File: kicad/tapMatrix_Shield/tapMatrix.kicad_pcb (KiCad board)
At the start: 2 copper layers, 68.6 x 53.3 mm, 28 parts, among them IC1 DS1307, P5 TS_ZIF, P6 LED_MATRIX_HDR, P7 SPKR, U1 APE8865N-33-HF-3, U2 MCP4921-E/SN, U3 74LS125, U4 TL072, U5 SD_CARD

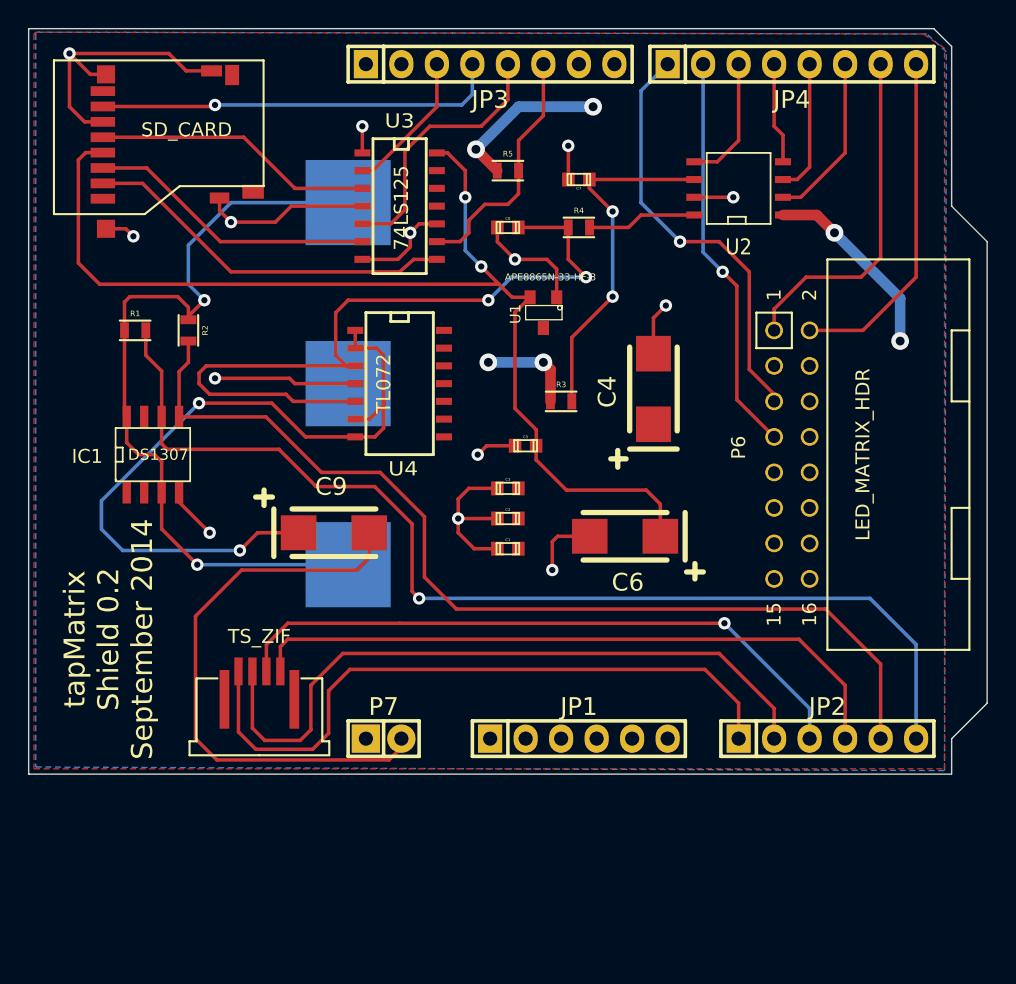
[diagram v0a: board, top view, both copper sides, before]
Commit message: added optional 4-pin header as alt for touchscreen zif
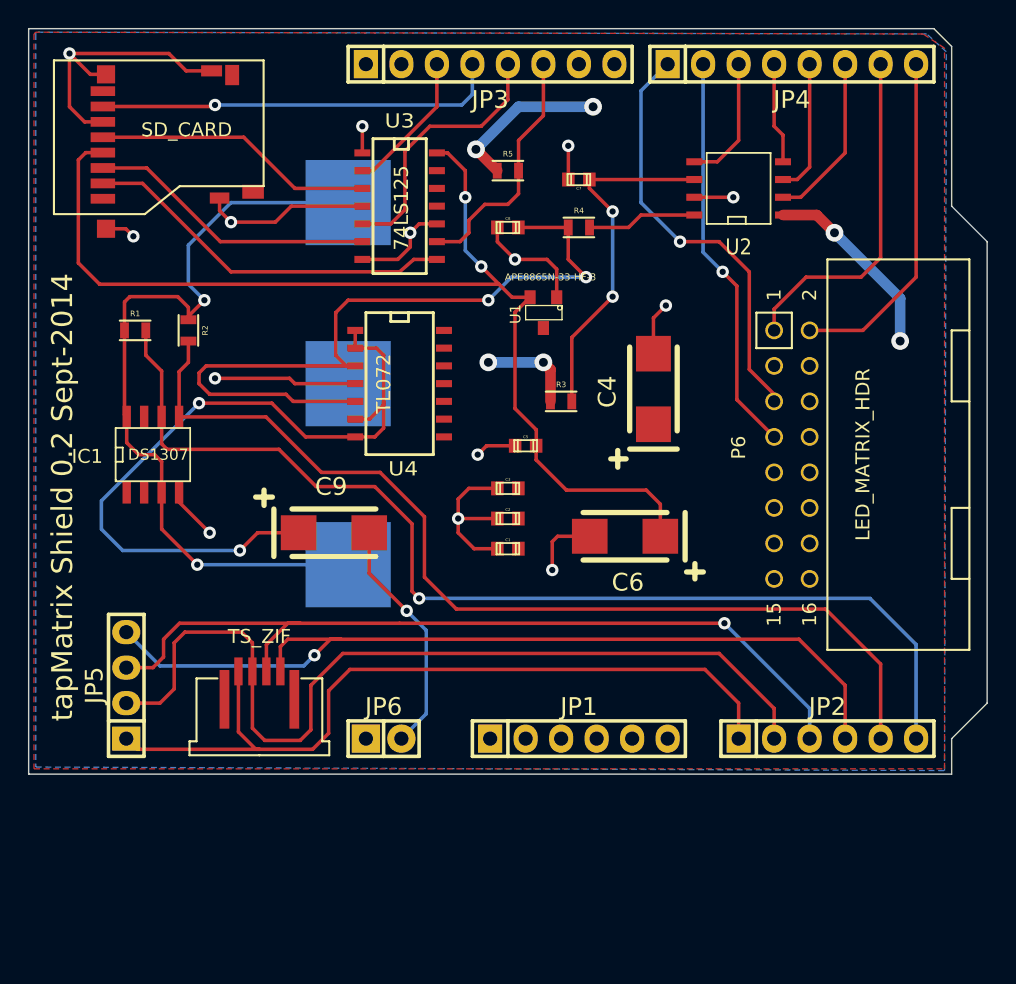
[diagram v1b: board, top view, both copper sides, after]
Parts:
- added JP5: 4_PIN_1, Pin_Headers:Pin_Header_Straight_1x04, F.Cu at (137.8, 133.3)
- renumbered P7 to JP6
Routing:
- net Net-(C9-Pad2): track 41.1 -> 17.8 mm, vias 0 -> 1
- net /YM: track 47.6 -> 64.7 mm, vias 0 -> 1
- net /YP: track 50.0 -> 65.4 mm
- net /XP: track 47.1 -> 61.6 mm
- net /XM: track 48.3 -> 58.2 mm
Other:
- board text added: "tapMatrix Shield 0.2 Sept-2014"
- board text removed: "tapMatrix Shield 0.2 September 2014"
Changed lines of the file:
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@@
 (kicad_pcb (version 4) (host pcbnew "(2014-08-05 BZR 5054)-product")
   (general
-    (links 85)
+    (links 89)
     (no_connects 0)
     (area 130.759999 86.309999 199.440001 139.750001)
     (thickness 1.6)
     (drawings 98)
-    (tracks 319)
+    (tracks 340)
     (zones 0)
-    (modules 28)
+    (modules 29)
     (nets 50)
   )
@@
     (descr "1 pin")
     (tags "CONN DEV")
-    (fp_text reference P7 (at 0 -2.286) (layer F.SilkS)
+    (fp_text reference JP6 (at 0 -2.286) (layer F.SilkS)
       (effects (font (size 1.27 1.27) (thickness 0.2032)))
     )
@@
       (net 5 "Net-(C9-Pad1)"))
   )
+  (module Pin_Headers:Pin_Header_Straight_1x04 (layer F.Cu)
+    (at 137.795 133.35 90)
+    (descr "1 pin")
+    (tags "CONN DEV")
+    (fp_text reference JP5 (at 0 -2.286 90) (layer F.SilkS)
+      (effects (font (size 1.27 1.27) (thickness 0.2032)))
+    )
+    (fp_text value 4_PIN_1 (at 0 0 90) (layer F.SilkS) hide
+      (effects (font (size 1.27 1.27) (thickness 0.2032)))
+    )
+    (fp_line (start -2.54 1.27) (end 5.08 1.27) (layer F.SilkS) (width 0.254))
+    (fp_line (start -2.54 -1.27) (end 5.08 -1.27) (layer F.SilkS) (width 0.254))
+    (fp_line (start -5.08 -1.27) (end -2.54 -1.27) (layer F.SilkS) (width 0.254))
+    (fp_line (start 5.08 1.27) (end 5.08 -1.27) (layer F.SilkS) (width 0.254))
+    (fp_line (start -2.54 -1.27) (end -2.54 1.27) (layer F.SilkS) (width 0.254))
+    (fp_line (start -5.08 -1.27) (end -5.08 1.27) (layer F.SilkS) (width 0.254))
+    (fp_line (start -5.08 1.27) (end -2.54 1.27) (layer F.SilkS) (width 0.254))
+    (pad 1 thru_hole rect (at -3.81 0 90) (size 1.7272 2.032) (drill 1.016) (layers *.Cu *.Mask F.SilkS)
+      (net 16 /XM))
+    (pad 2 thru_hole oval (at -1.27 0 90) (size 1.7272 2.032) (drill 1.016) (layers *.Cu *.Mask F.SilkS)
+      (net 17 /YP))
+    (pad 3 thru_hole oval (at 1.27 0 90) (size 1.7272 2.032) (drill 1.016) (layers *.Cu *.Mask F.SilkS)
+      (net 18 /XP))
+    (pad 4 thru_hole oval (at 3.81 0 90) (size 1.7272 2.032) (drill 1.016) (layers *.Cu *.Mask F.SilkS)
+      (net 19 /YM))
+    (model Pin_Headers/Pin_Header_Straight_1x04.wrl
+      (at (xyz 0 0 0))
+      (scale (xyz 1 1 1))
+      (rotate (xyz 0 0 0))
+    )
+  )
   (gr_text "(c) 2014 Responsive Devices Inc" (at 133.35 119.126 90) (layer B.SilkS)
     (effects (font (size 1.5 1.5) (thickness 0.3)) (justify mirror))
   )
-  (gr_text "tapMatrix\nShield 0.2\nSeptember 2014" (at 136.525 130.048 90) (layer F.SilkS)
+  (gr_text "tapMatrix Shield 0.2 Sept-2014" (at 133.223 119.888 90) (layer F.SilkS)
     (effects (font (size 1.5 1.5) (thickness 0.3)))
   )
@@
   (segment (start 156.21 114.935) (end 155.575 115.57) (width 0.254) (layer F.Cu) (net 5))
   (segment (start 155.575 115.57) (end 154.178 115.57) (width 0.254) (layer F.Cu) (net 5))
+  (segment (start 155.17876 122.428) (end 155.17876 125.33376) (width 0.254) (layer F.Cu) (net 6))
+  (segment (start 159.258 135.382) (end 157.48 137.16) (width 0.254) (layer B.Cu) (net 6))
+  (segment (start 159.258 129.413) (end 159.258 135.382) (width 0.254) (layer B.Cu) (net 6))
+  (segment (start 157.861 128.016) (end 159.258 129.413) (width 0.254) (layer B.Cu) (net 6))
+  (via (at 157.861 128.016) (size 0.889) (layers F.Cu B.Cu) (net 6))
+  (segment (start 155.17876 125.33376) (end 157.861 128.016) (width 0.254) (layer F.Cu) (net 6))
   (segment (start 157.48 137.16) (end 157.48 137.795) (width 0.254) (layer F.Cu) (net 6))
-  (segment (start 157.48 137.795) (end 156.591 138.684) (width 0.254) (layer F.Cu) (net 6))
-  (segment (start 156.591 138.684) (end 144.272 138.684) (width 0.254) (layer F.Cu) (net 6))
-  (segment (start 144.272 138.684) (end 142.748 137.16) (width 0.254) (layer F.Cu) (net 6))
-  (segment (start 142.748 137.16) (end 142.748 128.397) (width 0.254) (layer F.Cu) (net 6))
-  (segment (start 142.748 128.397) (end 146.05 125.095) (width 0.254) (layer F.Cu) (net 6))
-  (segment (start 146.05 125.095) (end 154.305 125.095) (width 0.254) (layer F.Cu) (net 6))
-  (segment (start 154.305 125.095) (end 155.17876 124.22124) (width 0.254) (layer F.Cu) (net 6))
-  (segment (start 155.17876 124.22124) (end 155.17876 122.428) (width 0.254) (layer F.Cu) (net 6))
   (segment (start 153.67 98.806) (end 145.288 98.806) (width 0.254) (layer B.Cu) (net 7))
   (segment (start 143.383 105.791) (end 142.24 106.934) (width 0.254) (layer F.Cu) (net 7))
@@
   (segment (start 141.575 110.901) (end 141.575 114.14) (width 0.254) (layer F.Cu) (net 11))
   (segment (start 142.24 110.236) (end 141.575 110.901) (width 0.254) (layer F.Cu) (net 11))
+  (segment (start 147.32 137.922) (end 138.557 137.922) (width 0.254) (layer F.Cu) (net 16))
+  (segment (start 138.557 137.922) (end 137.795 137.16) (width 0.254) (layer F.Cu) (net 16))
   (segment (start 181.61 137.16) (end 181.61 134.62) (width 0.254) (layer F.Cu) (net 16))
   (segment (start 145.82 136.676) (end 145.82 132.35) (width 0.254) (layer F.Cu) (net 16))
   (segment (start 147.066 137.922) (end 145.82 136.676) (width 0.254) (layer F.Cu) (net 16))
-  (segment (start 151.13 137.922) (end 147.066 137.922) (width 0.254) (layer F.Cu) (net 16))
+  (segment (start 151.13 137.922) (end 147.32 137.922) (width 0.254) (layer F.Cu) (net 16))
+  (segment (start 147.32 137.922) (end 147.066 137.922) (width 0.254) (layer F.Cu) (net 16))
   (segment (start 152.273 136.779) (end 151.13 137.922) (width 0.254) (layer F.Cu) (net 16))
   (segment (start 152.273 133.731) (end 152.273 136.779) (width 0.254) (layer F.Cu) (net 16))
@@
   (segment (start 179.197 132.207) (end 153.797 132.207) (width 0.254) (layer F.Cu) (net 16))
   (segment (start 181.61 134.62) (end 179.197 132.207) (width 0.254) (layer F.Cu) (net 16))
+  (segment (start 146.82 132.35) (end 146.82 130.31) (width 0.254) (layer F.Cu) (net 17))
+  (segment (start 140.208 134.62) (end 137.795 134.62) (width 0.254) (layer F.Cu) (net 17))
+  (segment (start 141.224 133.604) (end 140.208 134.62) (width 0.254) (layer F.Cu) (net 17))
+  (segment (start 141.224 130.302) (end 141.224 133.604) (width 0.254) (layer F.Cu) (net 17))
+  (segment (start 141.986 129.54) (end 141.224 130.302) (width 0.254) (layer F.Cu) (net 17))
+  (segment (start 146.05 129.54) (end 141.986 129.54) (width 0.254) (layer F.Cu) (net 17))
+  (segment (start 146.82 130.31) (end 146.05 129.54) (width 0.254) (layer F.Cu) (net 17))
   (segment (start 184.15 137.16) (end 184.15 135.001) (width 0.254) (layer F.Cu) (net 17))
   (segment (start 146.82 136.406) (end 146.82 132.35) (width 0.254) (layer F.Cu) (net 17))
@@
   (segment (start 184.15 135.001) (end 180.213 131.064) (width 0.254) (layer F.Cu) (net 17))
   (segment (start 146.812 132.342) (end 146.82 132.35) (width 0.254) (layer F.Cu) (net 17))
+  (segment (start 150.241 128.905) (end 141.605 128.905) (width 0.254) (layer F.Cu) (net 18))
+  (segment (start 139.7 132.08) (end 137.795 132.08) (width 0.254) (layer F.Cu) (net 18))
+  (segment (start 140.462 131.318) (end 139.7 132.08) (width 0.254) (layer F.Cu) (net 18))
+  (segment (start 140.462 130.048) (end 140.462 131.318) (width 0.254) (layer F.Cu) (net 18))
+  (segment (start 141.605 128.905) (end 140.462 130.048) (width 0.254) (layer F.Cu) (net 18))
   (segment (start 186.69 137.16) (end 186.69 135.001) (width 0.254) (layer B.Cu) (net 18))
   (segment (start 147.82 130.437) (end 147.82 132.35) (width 0.254) (layer F.Cu) (net 18))
   (segment (start 149.352 128.905) (end 147.82 130.437) (width 0.254) (layer F.Cu) (net 18))
-  (segment (start 157.353 128.905) (end 149.352 128.905) (width 0.254) (layer F.Cu) (net 18))
+  (segment (start 157.353 128.905) (end 150.241 128.905) (width 0.254) (layer F.Cu) (net 18))
+  (segment (start 150.241 128.905) (end 149.352 128.905) (width 0.254) (layer F.Cu) (net 18))
   (segment (start 180.594 128.905) (end 157.353 128.905) (width 0.254) (layer F.Cu) (net 18))
   (via (at 180.594 128.905) (size 0.889) (layers F.Cu B.Cu) (net 18))
@@
   (segment (start 147.955 132.215) (end 147.82 132.35) (width 0.254) (layer F.Cu) (net 18))
   (segment (start 186.69 137.16) (end 185.928 137.16) (width 0.254) (layer F.Cu) (net 18))
+  (segment (start 153.162 130.048) (end 152.4 130.048) (width 0.254) (layer F.Cu) (net 19))
+  (segment (start 140.208 131.953) (end 137.795 129.54) (width 0.254) (layer B.Cu) (net 19))
+  (segment (start 150.495 131.953) (end 140.208 131.953) (width 0.254) (layer B.Cu) (net 19))
+  (segment (start 151.257 131.191) (end 150.495 131.953) (width 0.254) (layer B.Cu) (net 19))
+  (via (at 151.257 131.191) (size 0.889) (layers F.Cu B.Cu) (net 19))
+  (segment (start 152.4 130.048) (end 151.257 131.191) (width 0.254) (layer F.Cu) (net 19))
   (segment (start 189.23 137.16) (end 189.23 133.35) (width 0.254) (layer F.Cu) (net 19))
   (segment (start 148.82 130.58) (end 148.82 132.35) (width 0.254) (layer F.Cu) (net 19))
   (segment (start 149.352 130.048) (end 148.82 130.58) (width 0.254) (layer F.Cu) (net 19))
-  (segment (start 185.928 130.048) (end 149.352 130.048) (width 0.254) (layer F.Cu) (net 19))
+  (segment (start 185.928 130.048) (end 153.162 130.048) (width 0.254) (layer F.Cu) (net 19))
+  (segment (start 153.162 130.048) (end 149.352 130.048) (width 0.254) (layer F.Cu) (net 19))
   (segment (start 189.23 133.35) (end 185.928 130.048) (width 0.254) (layer F.Cu) (net 19))
   (segment (start 160.02 88.9) (end 160.02 91.948) (width 0.254) (layer F.Cu) (net 21))
